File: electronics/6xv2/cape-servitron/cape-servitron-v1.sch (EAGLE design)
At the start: 100 parts, among them IC1 74541PW, IC2 74541PW, IC3 74541PW, IC4 LM2574M-5.0, M0-CONN PINHEAD-5MM-1X2, M0-CONN1 PINHEAD-5MM-1X2, M0-CONN2 PINHEAD-5MM-1X2, M0-CONN3 PINHEAD-5MM-1X2, M0-CONN4 PINHEAD-5MM-1X2, M0-CONN5 PINHEAD-5MM-1X2, Q1 BSS123

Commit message: added holes, layout mostly done
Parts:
- added H1, H2, H3, H4: MOUNT-HOLE3.0, holes:MOUNT-HOLE3.0
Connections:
- net N$19: now also U$4.P$4; no longer U$4.P$3
- net N$20: now also U$4.P$3; no longer U$4.P$4
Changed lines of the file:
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@@
 <part name="P+20" library="supply1" deviceset="VCC" device=""/>
 <part name="P+21" library="supply1" deviceset="VCC" device=""/>
+<part name="H1" library="holes" deviceset="MOUNT-HOLE" device="3.0"/>
+<part name="H2" library="holes" deviceset="MOUNT-HOLE" device="3.0"/>
+<part name="H3" library="holes" deviceset="MOUNT-HOLE" device="3.0"/>
+<part name="H4" library="holes" deviceset="MOUNT-HOLE" device="3.0"/>
 </parts>
 <sheets>
@@
 <instance part="R4" gate="G$1" x="132.08" y="116.84" rot="R90"/>
 <instance part="R5" gate="G$1" x="124.46" y="116.84" rot="R90"/>
-<instance part="U$4" gate="G$1" x="134.62" y="86.36"/>
+<instance part="U$4" gate="G$1" x="137.16" y="86.36" rot="MR0"/>
 <instance part="R6" gate="G$1" x="147.32" y="116.84" rot="R90"/>
 <instance part="U$5" gate="G$1" x="139.7" y="27.94" rot="MR0"/>
@@
 <pinref part="U$3" gate="G$1" pin="VSS"/>
 <wire x1="170.18" y1="68.58" x2="170.18" y2="73.66" width="0.1524" layer="91"/>
+<wire x1="170.18" y1="73.66" x2="170.18" y2="91.44" width="0.1524" layer="91"/>
+<pinref part="U$4" gate="G$1" pin="P$2"/>
 <pinref part="U$4" gate="G$1" pin="P$1"/>
-<pinref part="U$4" gate="G$1" pin="P$2"/>
-<wire x1="170.18" y1="73.66" x2="170.18" y2="91.44" width="0.1524" layer="91"/>
-<wire x1="132.08" y1="73.66" x2="139.7" y2="73.66" width="0.1524" layer="91"/>
+<wire x1="139.7" y1="73.66" x2="132.08" y2="73.66" width="0.1524" layer="91"/>
 <wire x1="139.7" y1="73.66" x2="170.18" y2="73.66" width="0.1524" layer="91"/>
 <junction x="139.7" y="73.66"/>
@@
 <pinref part="U$3" gate="G$1" pin="A0"/>
 <wire x1="139.7" y1="109.22" x2="152.4" y2="109.22" width="0.1524" layer="91"/>
-<wire x1="139.7" y1="109.22" x2="139.7" y2="101.6" width="0.1524" layer="91"/>
+<pinref part="U$4" gate="G$1" pin="P$4"/>
+<wire x1="139.7" y1="101.6" x2="139.7" y2="109.22" width="0.1524" layer="91"/>
 <junction x="139.7" y="109.22"/>
-<pinref part="U$4" gate="G$1" pin="P$3"/>
 </segment>
 </net>
@@
 <wire x1="152.4" y1="106.68" x2="132.08" y2="106.68" width="0.1524" layer="91"/>
 <wire x1="132.08" y1="106.68" x2="132.08" y2="111.76" width="0.1524" layer="91"/>
-<wire x1="132.08" y1="106.68" x2="132.08" y2="101.6" width="0.1524" layer="91"/>
+<pinref part="U$4" gate="G$1" pin="P$3"/>
+<wire x1="132.08" y1="101.6" x2="132.08" y2="106.68" width="0.1524" layer="91"/>
 <junction x="132.08" y="106.68"/>
-<pinref part="U$4" gate="G$1" pin="P$4"/>
 </segment>
 </net>
@@
 </nets>
 </sheet>
+<sheet>
+<plain>
+</plain>
+<instances>
+<instance part="H1" gate="G$1" x="-35.56" y="96.52"/>
+<instance part="H2" gate="G$1" x="-35.56" y="88.9"/>
+<instance part="H3" gate="G$1" x="-35.56" y="81.28"/>
+<instance part="H4" gate="G$1" x="-35.56" y="73.66"/>
+</instances>
+<busses>
+</busses>
+<nets>
+</nets>
+</sheet>

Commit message: renamed chips and output signals to match board placement and markings
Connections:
- net OUT0A renamed OUT-5B
- net OUT0B renamed OUT-5A
- net OUT1A renamed OUT-4B
- net OUT1B renamed OUT-4A
- net OUT2A renamed OUT-1B
- net OUT2B renamed OUT-1A
- net OUT3A renamed OUT-0B
- net OUT3B renamed OUT-0A
- net OUT4A renamed OUT-3B
- net OUT4B renamed OUT-3A
- net OUT5A renamed OUT-2B
- net OUT5B renamed OUT-2A
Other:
- note added: "MOTOR 0"
- note added: "MOTOR 1"
- note added: "MOTOR 2"
- note added: "MOTOR 3"
- note added: "MOTOR 4"
- note added: "MOTOR 5"
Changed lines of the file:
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@@
 <sheet>
 <plain>
+<text x="86.36" y="160.02" size="3.81" layer="97">MOTOR 5</text>
+<text x="190.5" y="160.02" size="3.81" layer="97">MOTOR 4</text>
+<text x="297.18" y="160.02" size="3.81" layer="97">MOTOR 1</text>
+<text x="401.32" y="160.02" size="3.81" layer="97">MOTOR 0</text>
+<text x="403.86" y="2.54" size="3.81" layer="97">MOTOR 0</text>
+<text x="86.36" y="17.78" size="3.81" layer="97">MOTOR 3</text>
+<text x="190.5" y="17.78" size="3.81" layer="97">MOTOR 2</text>
 </plain>
 <instances>
@@
 </segment>
 </net>
-<net name="OUT0A" class="1">
+<net name="OUT-5B" class="1">
 <segment>
 <pinref part="U$6" gate="G$1" pin="OUT_A"/>
@@
 </segment>
 </net>
-<net name="OUT0B" class="1">
+<net name="OUT-5A" class="1">
 <segment>
 <pinref part="U$6" gate="G$1" pin="OUT_B"/>
@@
 </segment>
 </net>
-<net name="OUT1A" class="1">
+<net name="OUT-4B" class="1">
 <segment>
 <pinref part="U$7" gate="G$1" pin="OUT_A"/>
@@
 </segment>
 </net>
-<net name="OUT1B" class="1">
+<net name="OUT-4A" class="1">
 <segment>
 <pinref part="U$7" gate="G$1" pin="OUT_B"/>
@@
 </segment>
 </net>
-<net name="OUT2A" class="1">
+<net name="OUT-1B" class="1">
 <segment>
 <pinref part="U$8" gate="G$1" pin="OUT_A"/>
@@
 </segment>
 </net>
-<net name="OUT2B" class="1">
+<net name="OUT-1A" class="1">
 <segment>
 <pinref part="U$8" gate="G$1" pin="OUT_B"/>
@@
 </segment>
 </net>
-<net name="OUT3A" class="1">
+<net name="OUT-0B" class="1">
 <segment>
 <pinref part="U$9" gate="G$1" pin="OUT_A"/>
@@
 </segment>
 </net>
-<net name="OUT3B" class="1">
+<net name="OUT-0A" class="1">
 <segment>
 <pinref part="U$9" gate="G$1" pin="OUT_B"/>
@@
 </segment>
 </net>
-<net name="OUT4A" class="1">
+<net name="OUT-3B" class="1">
 <segment>
 <pinref part="U$10" gate="G$1" pin="OUT_A"/>
@@
 </segment>
 </net>
-<net name="OUT4B" class="1">
+<net name="OUT-3A" class="1">
 <segment>
 <pinref part="U$10" gate="G$1" pin="OUT_B"/>
@@
 </segment>
 </net>
-<net name="OUT5A" class="1">
+<net name="OUT-2B" class="1">
 <segment>
 <pinref part="U$11" gate="G$1" pin="OUT_A"/>
@@
 </segment>
 </net>
-<net name="OUT5B" class="1">
+<net name="OUT-2A" class="1">
 <segment>
 <pinref part="U$11" gate="G$1" pin="OUT_B"/>
@@
 </segment>
 </net>
-<net name="OUT0A" class="1">
+<net name="OUT-5B" class="1">
 <segment>
 <wire x1="27.94" y1="88.9" x2="20.32" y2="88.9" width="0.1524" layer="91"/>
@@
 </segment>
 </net>
-<net name="OUT0B" class="1">
+<net name="OUT-5A" class="1">
 <segment>
 <wire x1="27.94" y1="83.82" x2="20.32" y2="83.82" width="0.1524" layer="91"/>
@@
 </segment>
 </net>
-<net name="OUT1A" class="1">
+<net name="OUT-4B" class="1">
 <segment>
 <wire x1="20.32" y1="78.74" x2="27.94" y2="78.74" width="0.1524" layer="91"/>
@@
 </segment>
 </net>
-<net name="OUT1B" class="1">
+<net name="OUT-4A" class="1">
 <segment>
 <wire x1="20.32" y1="73.66" x2="27.94" y2="73.66" width="0.1524" layer="91"/>
@@
 </segment>
 </net>
-<net name="OUT2A" class="1">
+<net name="OUT-1B" class="1">
 <segment>
 <wire x1="20.32" y1="68.58" x2="27.94" y2="68.58" width="0.1524" layer="91"/>
@@
 </segment>
 </net>
-<net name="OUT2B" class="1">
+<net name="OUT-1A" class="1">
 <segment>
 <wire x1="20.32" y1="63.5" x2="27.94" y2="63.5" width="0.1524" layer="91"/>
@@
 </segment>
 </net>
-<net name="OUT3A" class="1">
+<net name="OUT-0B" class="1">
 <segment>
 <wire x1="20.32" y1="58.42" x2="27.94" y2="58.42" width="0.1524" layer="91"/>
@@
 </segment>
 </net>
-<net name="OUT3B" class="1">
+<net name="OUT-0A" class="1">
 <segment>
 <wire x1="20.32" y1="53.34" x2="27.94" y2="53.34" width="0.1524" layer="91"/>
@@
 </segment>
 </net>
-<net name="OUT4A" class="1">
+<net name="OUT-3B" class="1">
 <segment>
 <wire x1="20.32" y1="48.26" x2="27.94" y2="48.26" width="0.1524" layer="91"/>
@@
 </segment>
 </net>
-<net name="OUT4B" class="1">
+<net name="OUT-3A" class="1">
 <segment>
 <wire x1="20.32" y1="43.18" x2="27.94" y2="43.18" width="0.1524" layer="91"/>
@@
 </segment>
 </net>
-<net name="OUT5A" class="1">
+<net name="OUT-2B" class="1">
 <segment>
 <wire x1="20.32" y1="38.1" x2="27.94" y2="38.1" width="0.1524" layer="91"/>
@@
 </segment>
 </net>
-<net name="OUT5B" class="1">
+<net name="OUT-2A" class="1">
 <segment>
 <wire x1="20.32" y1="33.02" x2="27.94" y2="33.02" width="0.1524" layer="91"/>

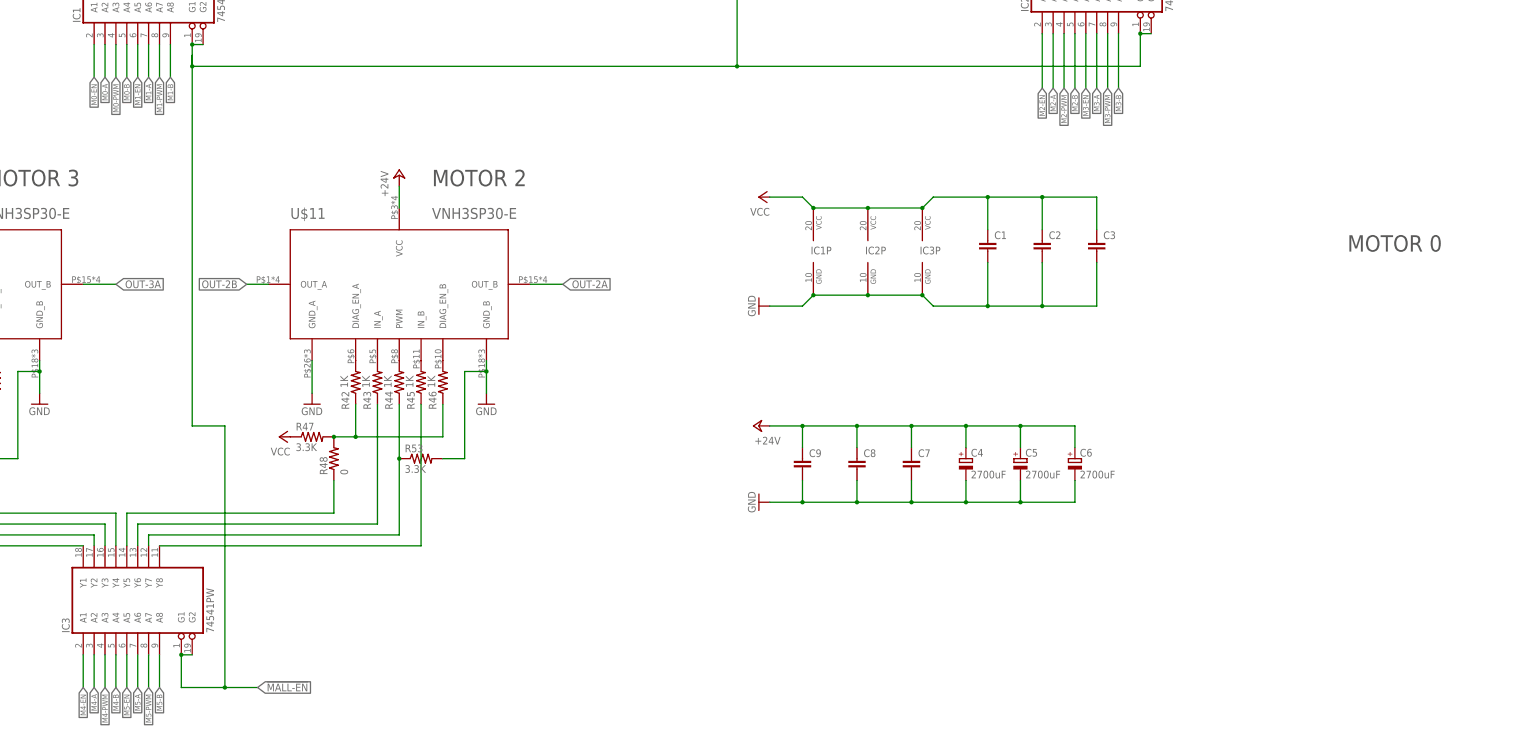
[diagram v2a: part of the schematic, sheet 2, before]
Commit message: updated signals for current layout
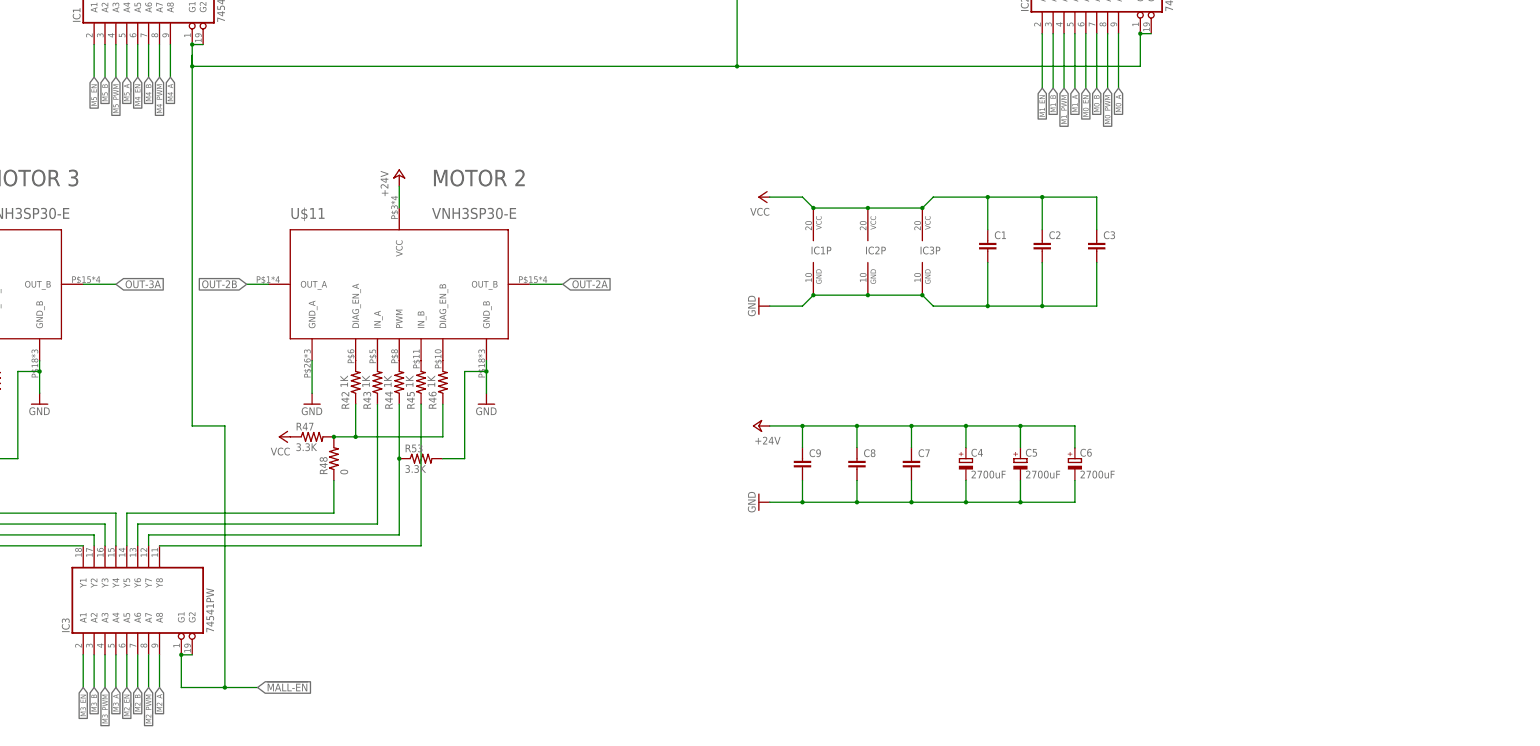
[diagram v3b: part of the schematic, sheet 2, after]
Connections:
- net M0-A renamed M5_B
- net M0-B renamed M5_A
- net M0-EN renamed M5_EN
- net M0-PWM renamed M5_PWM
- net M1-A renamed M4_B
- net M1-B renamed M4_A
- net M1-EN renamed M4_EN
- net M1-PWM renamed M4_PWM
- net M2-A renamed M1_B
- net M2-B renamed M1_A
- net M2-EN renamed M1_EN
- net M2-PWM renamed M1_PWM
- net M3-A renamed M0_B
- net M3-B renamed M0_A
- net M3-EN renamed M0_EN
- net M3-PWM renamed M0_PWM
- net M4-A renamed M3_B
- net M4-B renamed M3_A
- net M4-EN renamed M3_EN
- net M4-PWM renamed M3_PWM
- net M5-A renamed M2_B
- net M5-B renamed M2_A
- net M5-EN renamed M2_EN
- net M5-PWM renamed M2_PWM
